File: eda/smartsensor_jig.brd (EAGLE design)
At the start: 33 x 27.9 mm, 12 parts, among them J2 AVR_SPI_PRG_6PTH

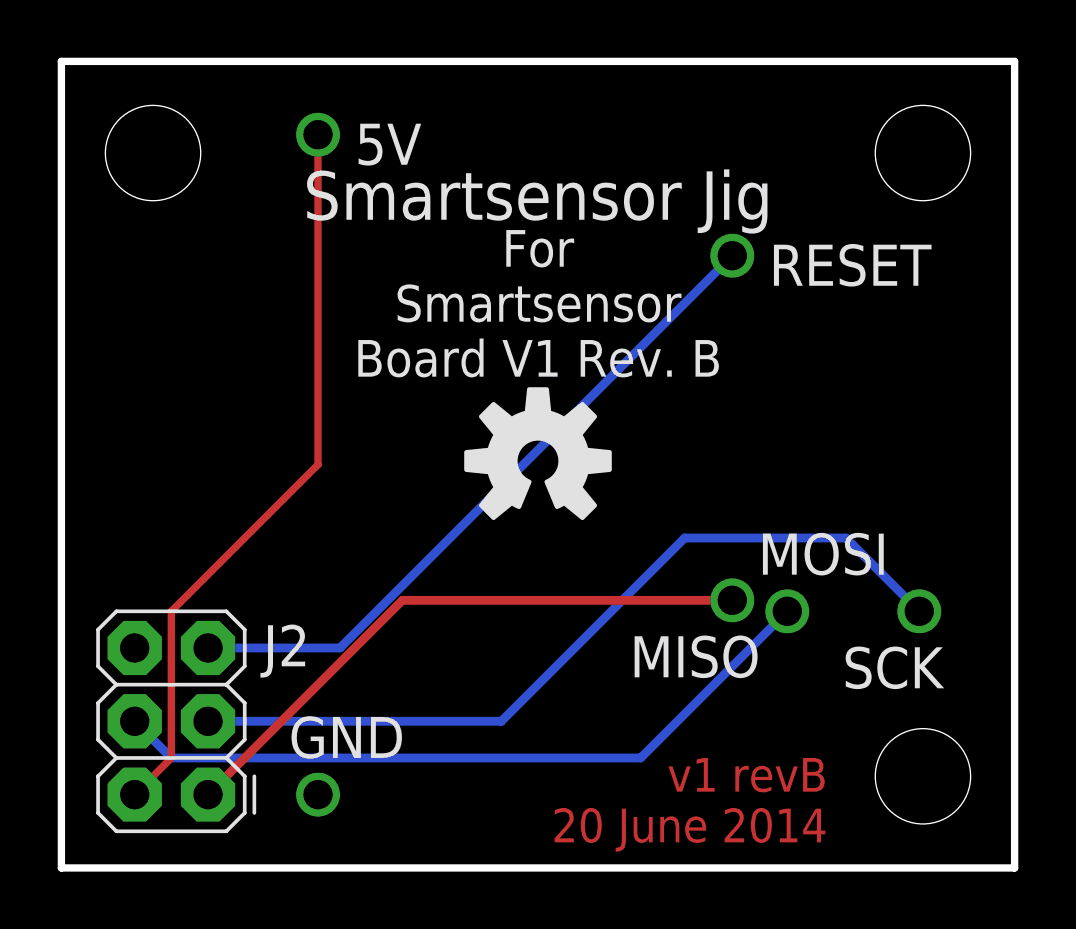
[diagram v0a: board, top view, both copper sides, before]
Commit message: Replaced 2x4 connectors with 2x5's.
On smartsensor, smartsensorPowered, smartsensor_powered_jig, and team_flag.
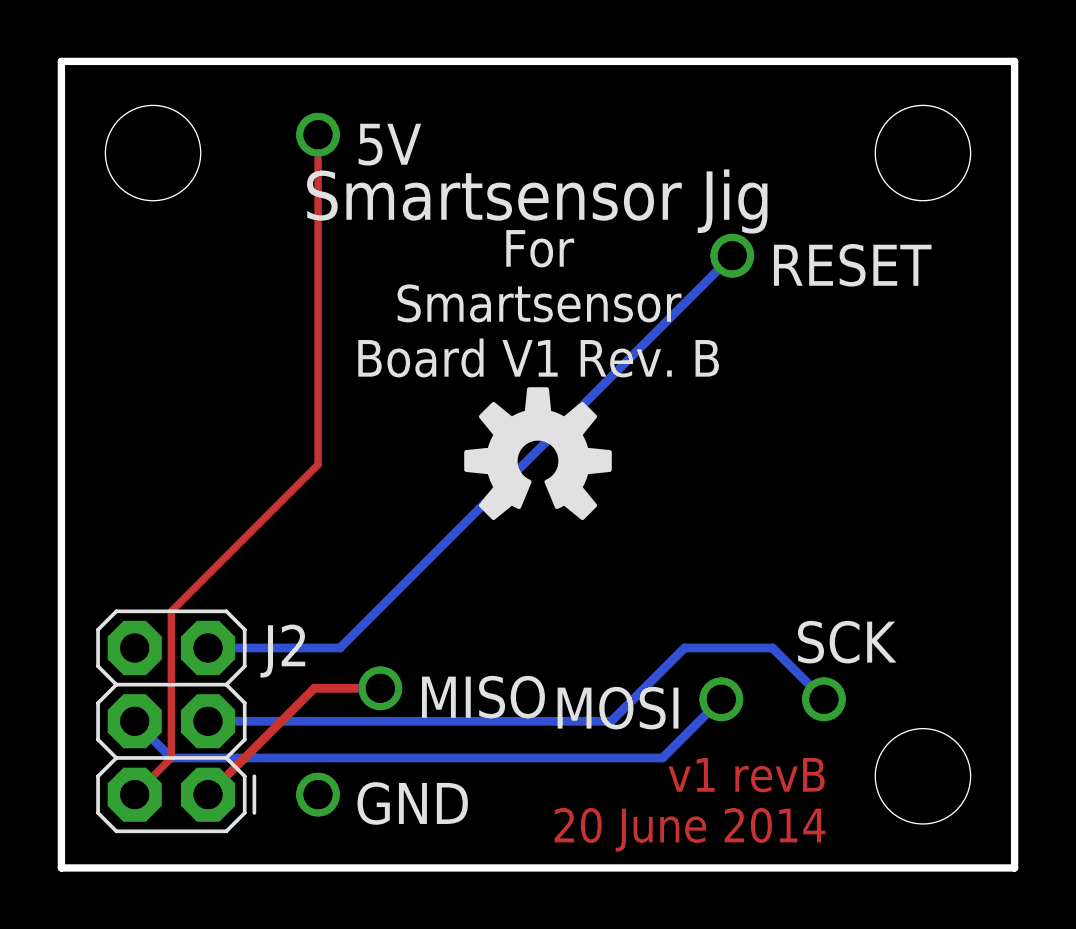
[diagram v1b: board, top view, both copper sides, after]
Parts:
- moved MISO 12.6 mm to (11.0, 6.22)
- moved SCK 4.49 mm to (26.4, 5.84)
- moved MOSI 3.81 mm to (22.9, 5.84)
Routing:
- net MISO: track 20.9 -> 7.49 mm
- net SCK: track 28.3 -> 23.1 mm
- net MOSI: track 25.2 -> 21.7 mm
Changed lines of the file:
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@@
 <attribute name="PIE-INT-REF-NUM" value="BULK-STOCK" x="5.08" y="2.54" size="1.778" layer="27" rot="R90" display="off"/>
 </element>
-<element name="MISO" library="pie" package="POGO_PIN_394" value="" x="23.241" y="9.271" smashed="yes">
-<attribute name="NAME" x="19.685" y="6.604" size="1.4224" layer="25" font="vector" ratio="15"/>
-<attribute name="VALUE" x="21.971" y="6.731" size="1.27" layer="27" font="vector"/>
-<attribute name="PIE-INT-REF-NUM" value="POGO-PIN" x="23.241" y="9.271" size="1.778" layer="27" display="off"/>
+<element name="MISO" library="pie" package="POGO_PIN_394" value="" x="11.049" y="6.223" smashed="yes">
+<attribute name="NAME" x="12.319" y="5.207" size="1.4224" layer="25" font="vector" ratio="15"/>
+<attribute name="VALUE" x="9.779" y="3.683" size="1.27" layer="27" font="vector"/>
+<attribute name="PIE-INT-REF-NUM" value="POGO-PIN" x="11.049" y="6.223" size="1.778" layer="27" display="off"/>
 </element>
-<element name="SCK" library="pie" package="POGO_PIN_394" value="" x="29.718" y="8.89" smashed="yes">
-<attribute name="NAME" x="27.051" y="6.223" size="1.4224" layer="25" font="vector" ratio="15"/>
-<attribute name="VALUE" x="28.448" y="6.35" size="1.27" layer="27" font="vector"/>
-<attribute name="PIE-INT-REF-NUM" value="POGO-PIN" x="29.718" y="8.89" size="1.778" layer="27" display="off"/>
+<element name="SCK" library="pie" package="POGO_PIN_394" value="" x="26.416" y="5.842" smashed="yes">
+<attribute name="NAME" x="25.4" y="7.112" size="1.4224" layer="25" font="vector" ratio="15"/>
+<attribute name="VALUE" x="25.146" y="3.302" size="1.27" layer="27" font="vector"/>
+<attribute name="PIE-INT-REF-NUM" value="POGO-PIN" x="26.416" y="5.842" size="1.778" layer="27" display="off"/>
 </element>
 <element name="RESET" library="pie" package="POGO_PIN_394" value="" x="23.241" y="21.209" smashed="yes" rot="R270">
@@
 <attribute name="PIE-INT-REF-NUM" value="POGO-PIN" x="8.89" y="25.4" size="1.778" layer="27" rot="R270" display="off"/>
 </element>
-<element name="MOSI" library="pie" package="POGO_PIN_394" value="" x="25.146" y="8.89" smashed="yes">
-<attribute name="NAME" x="24.13" y="10.16" size="1.4224" layer="25" font="vector" ratio="15"/>
-<attribute name="VALUE" x="23.876" y="6.35" size="1.27" layer="27" font="vector"/>
-<attribute name="PIE-INT-REF-NUM" value="POGO-PIN" x="25.146" y="8.89" size="1.778" layer="27" display="off"/>
+<element name="MOSI" library="pie" package="POGO_PIN_394" value="" x="22.86" y="5.842" smashed="yes">
+<attribute name="NAME" x="17.018" y="4.826" size="1.4224" layer="25" font="vector" ratio="15"/>
+<attribute name="VALUE" x="21.59" y="3.302" size="1.27" layer="27" font="vector"/>
+<attribute name="PIE-INT-REF-NUM" value="POGO-PIN" x="22.86" y="5.842" size="1.778" layer="27" display="off"/>
 </element>
 <element name="GND" library="pie" package="POGO_PIN_394" value="" x="8.89" y="2.54" smashed="yes" rot="R90">
-<attribute name="NAME" x="7.874" y="3.81" size="1.4224" layer="25" font="vector" ratio="15"/>
+<attribute name="NAME" x="10.16" y="1.524" size="1.4224" layer="25" font="vector" ratio="15"/>
 <attribute name="VALUE" x="11.43" y="1.27" size="1.27" layer="27" font="vector" rot="R90"/>
 <attribute name="PIE-INT-REF-NUM" value="POGO-PIN" x="8.89" y="2.54" size="1.778" layer="27" rot="R90" display="off"/>
@@
 <contactref element="MOSI" pad="POGO_PIN"/>
 <wire x1="2.54" y1="5.08" x2="3.81" y2="3.81" width="0.3048" layer="16"/>
-<wire x1="3.81" y1="3.81" x2="20.066" y2="3.81" width="0.3048" layer="16"/>
-<wire x1="20.066" y1="3.81" x2="25.146" y2="8.89" width="0.3048" layer="16"/>
+<wire x1="3.81" y1="3.81" x2="20.828" y2="3.81" width="0.3048" layer="16"/>
+<wire x1="20.828" y1="3.81" x2="22.86" y2="5.842" width="0.3048" layer="16"/>
 </signal>
 <signal name="5V">
@@
 <contactref element="J2" pad="3"/>
 <contactref element="SCK" pad="POGO_PIN"/>
-<wire x1="5.08" y1="5.08" x2="15.24" y2="5.08" width="0.3048" layer="16"/>
-<wire x1="15.24" y1="5.08" x2="21.59" y2="11.43" width="0.3048" layer="16"/>
-<wire x1="21.59" y1="11.43" x2="27.178" y2="11.43" width="0.3048" layer="16"/>
-<wire x1="27.178" y1="11.43" x2="29.718" y2="8.89" width="0.3048" layer="16"/>
+<wire x1="5.08" y1="5.08" x2="19.05" y2="5.08" width="0.3048" layer="16"/>
+<wire x1="19.05" y1="5.08" x2="21.59" y2="7.62" width="0.3048" layer="16"/>
+<wire x1="21.59" y1="7.62" x2="24.638" y2="7.62" width="0.3048" layer="16"/>
+<wire x1="24.638" y1="7.62" x2="26.416" y2="5.842" width="0.3048" layer="16"/>
 </signal>
 <signal name="MISO">
 <contactref element="J2" pad="1"/>
 <contactref element="MISO" pad="POGO_PIN"/>
-<wire x1="23.241" y1="9.271" x2="11.811" y2="9.271" width="0.3048" layer="1"/>
-<wire x1="11.811" y1="9.271" x2="5.08" y2="2.54" width="0.3048" layer="1"/>
+<wire x1="11.049" y1="6.223" x2="8.763" y2="6.223" width="0.3048" layer="1"/>
+<wire x1="8.763" y1="6.223" x2="5.08" y2="2.54" width="0.3048" layer="1"/>
 </signal>
 <signal name="GND">
@@
 </signal>
 </signals>
-<errors>
-</errors>
 </board>
 </drawing>
